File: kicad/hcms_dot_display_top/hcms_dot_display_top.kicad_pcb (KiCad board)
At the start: 4 copper layers, 35.6 x 19.8 mm, 27 parts, among them J1 Conn_01x12, J3 Conn_01x12, J4 Conn_01x11_Male, J6 Conn_01x12, J7 Conn_01x12, Q1 Q_PMOS_GSD, Q2 Q_PMOS_GSD, Q3 Q_PMOS_GSD, Q4 Q_PMOS_GSD, Q5 Q_PMOS_GSD

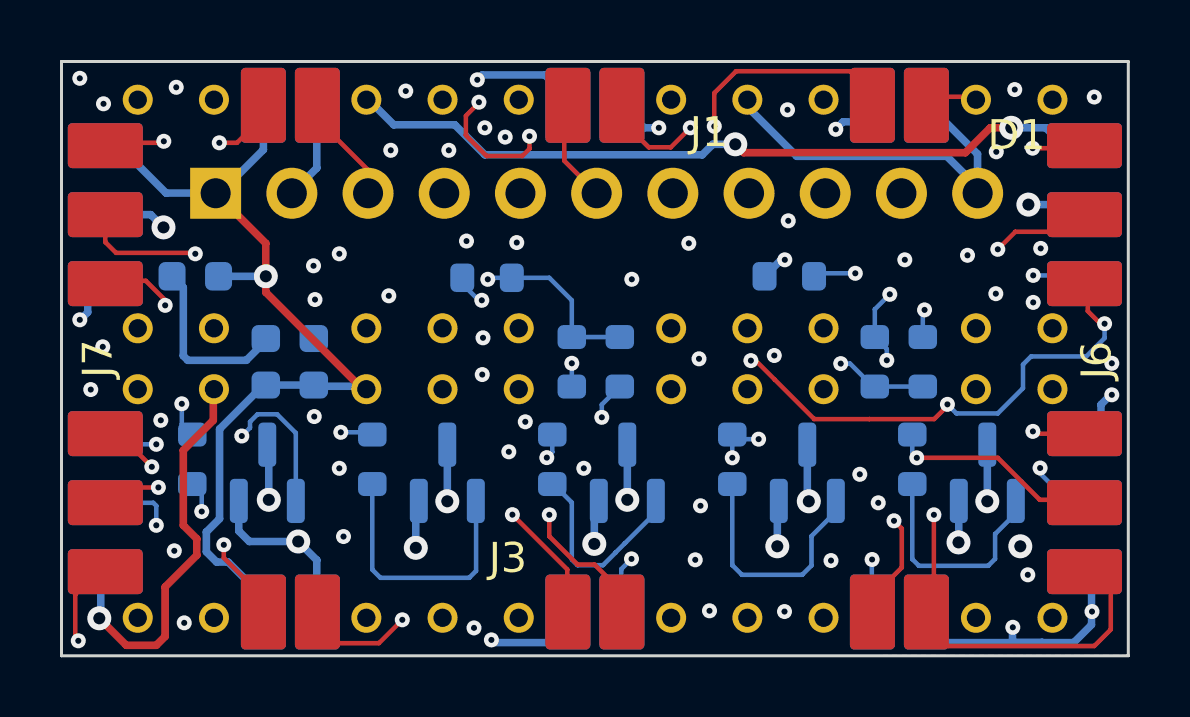
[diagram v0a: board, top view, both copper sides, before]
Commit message: Fixed daisy issue left right
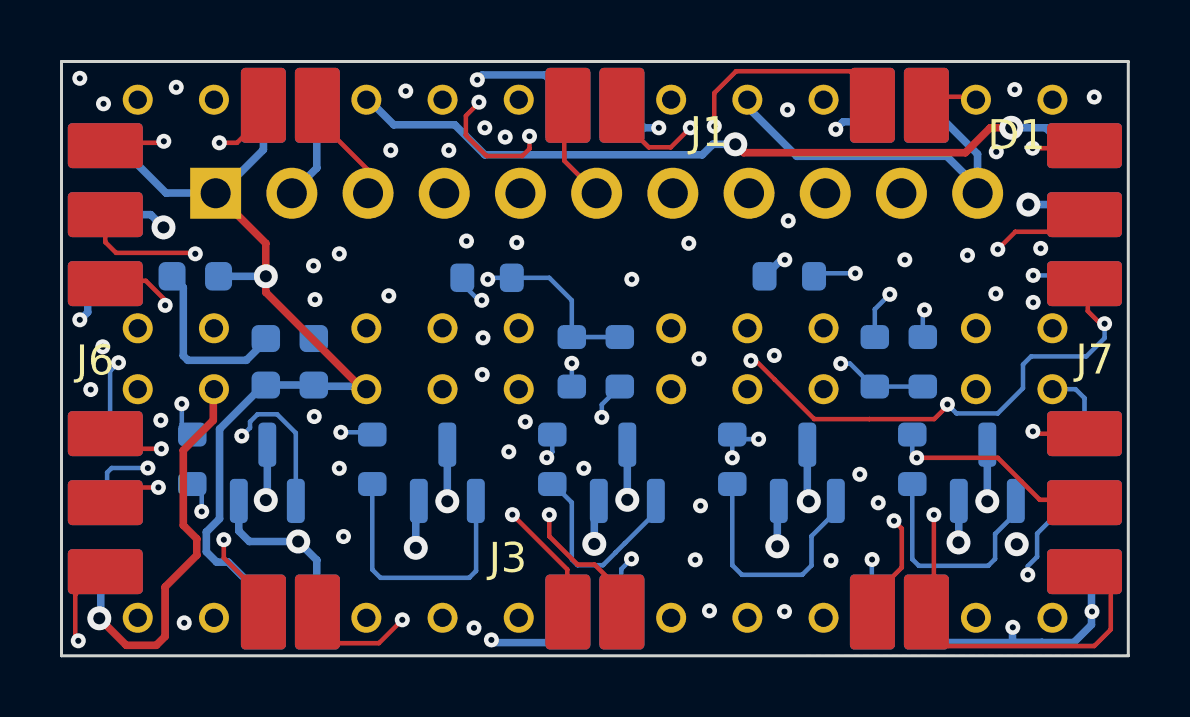
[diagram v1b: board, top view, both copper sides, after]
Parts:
- moved J6 32.6 mm to (143.9, 106.1)
- moved J7 32.6 mm to (176.6, 106.1)
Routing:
- net /B_DATA: track 52.6 -> 27.8 mm, vias 3 -> 2
- net /A_DATA: track 46.1 -> 27.0 mm, vias 4 -> 2
- net /DAISY_B_DATA: track 37.5 -> 50.0 mm
- net /DAISY_A_DATA: track 35.2 -> 40.1 mm, vias 7 -> 5
- net /MCU_COL_4: track 72.8 -> 71.9 mm
- net /MCU_COL_5: track 67.9 -> 68.7 mm
